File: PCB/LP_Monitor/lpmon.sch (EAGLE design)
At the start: 2 parts, among them U1 ATMEGA328P-PU

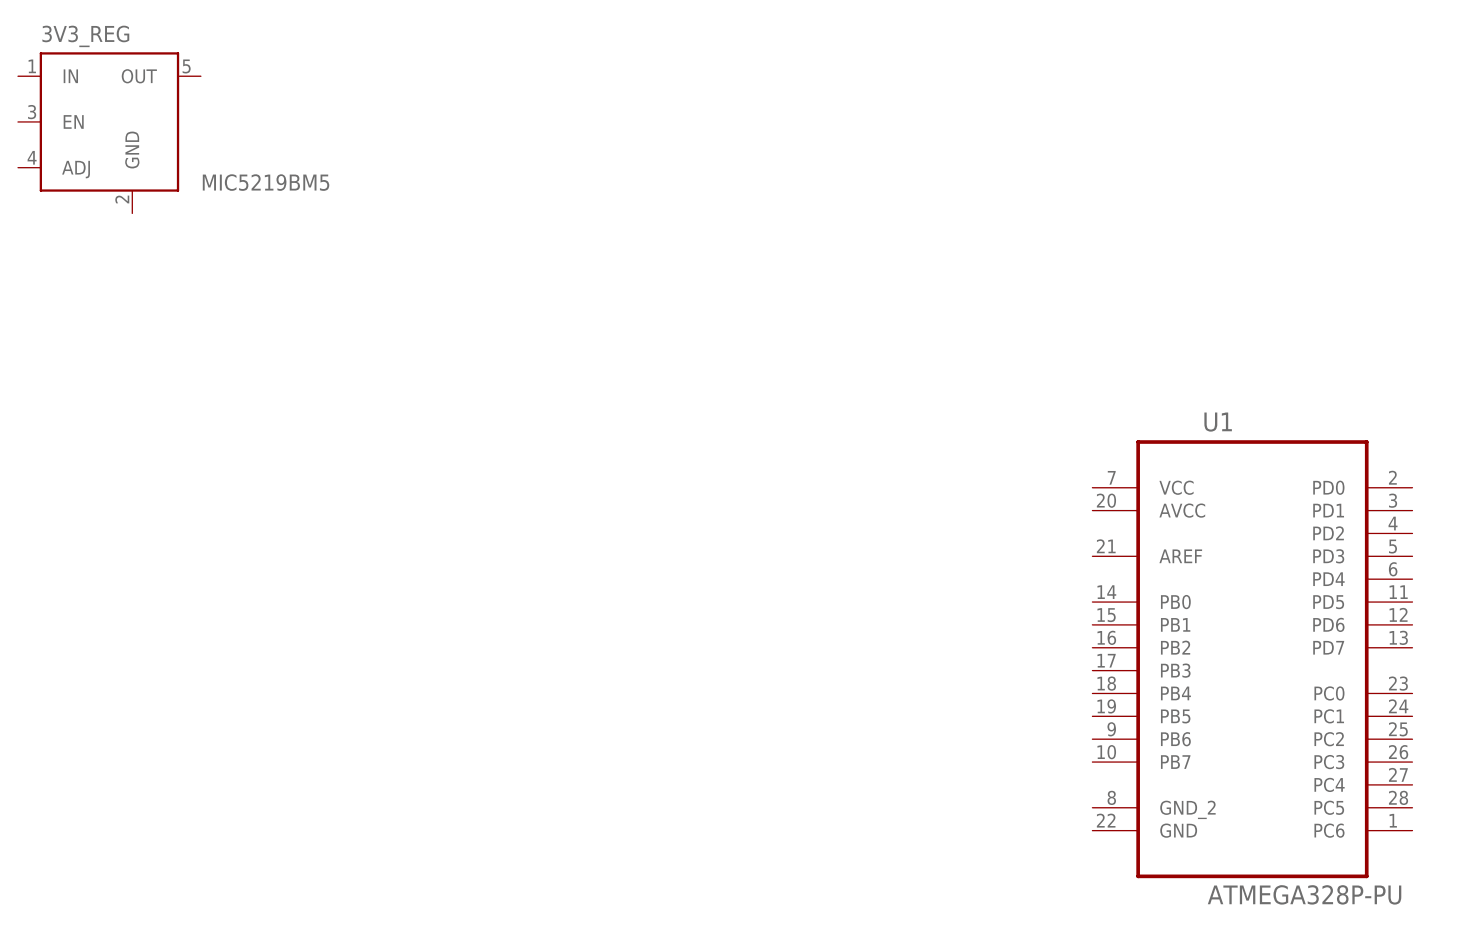
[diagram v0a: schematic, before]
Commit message: Arduino low power librarires
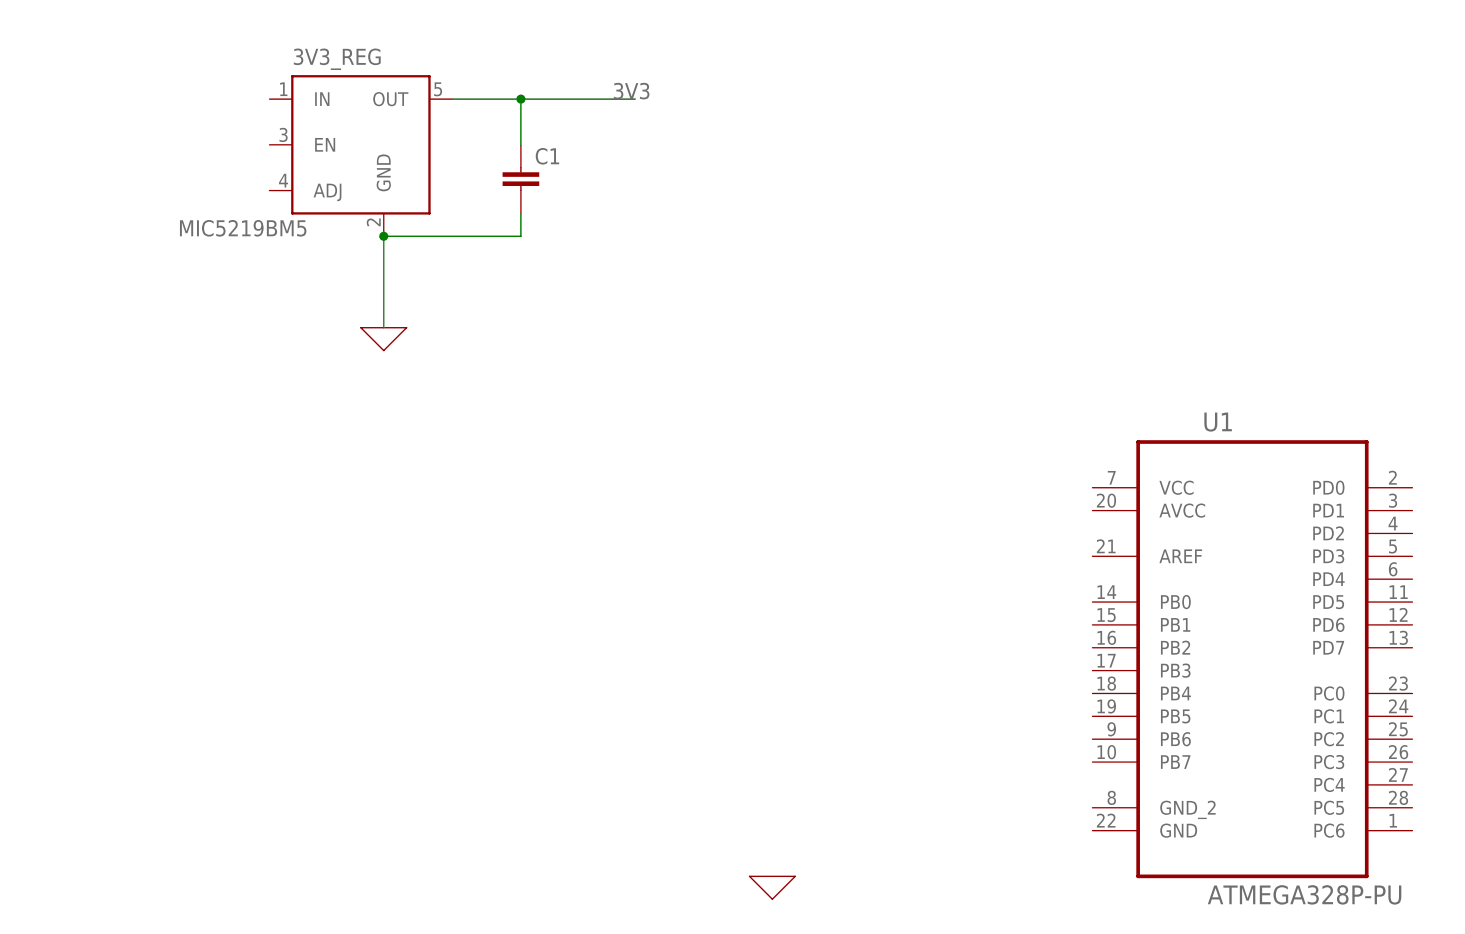
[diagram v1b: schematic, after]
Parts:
- added C1: (no value), capacitor-wima:C2.5/2
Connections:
- new net 0: 3V3_REG.GND, C1.2
- new net 3V3: 3V3_REG.OUT, C1.1
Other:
- moved on the sheet: 3V3_REG
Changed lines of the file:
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@@
 <layer number="97" name="Info" color="7" fill="1" visible="yes" active="yes"/>
 <layer number="98" name="Guide" color="6" fill="1" visible="yes" active="yes"/>
+<layer number="99" name="SpiceOrder" color="7" fill="1" visible="yes" active="yes"/>
 </layers>
 <schematic xreflabel="%F%N/%S.%C%R" xrefpart="/%S.%C%R">
@@
 <part name="U1" library="Atmel_By_element14_Batch_1-00" deviceset="ATMEGA328P-PU" device=""/>
 <part name="3V3_REG" library="v-reg-micrel" library_urn="urn:adsk.eagle:library:408" deviceset="MIC5219BM5" device="" package3d_urn="urn:adsk.eagle:package:30272/1"/>
+<part name="X_1" library="ngspice-simulation" library_urn="urn:adsk.eagle:library:527439" deviceset="GND" device=""/>
+<part name="X_2" library="ngspice-simulation" library_urn="urn:adsk.eagle:library:527439" deviceset="GND" device=""/>
+<part name="C1" library="capacitor-wima" library_urn="urn:adsk.eagle:library:116" deviceset="C" device="2.5/2" package3d_urn="urn:adsk.eagle:package:5415/1"/>
 </parts>
 <sheets>
@@
 <attribute name="VALUE" x="58.5216" y="32.4612" size="2.0828" layer="96" ratio="10" rot="SR0"/>
 </instance>
-<instance part="3V3_REG" gate="G1" x="-63.5" y="119.38" smashed="yes">
-<attribute name="NAME" x="-71.12" y="128.27" size="1.778" layer="95"/>
-<attribute name="VALUE" x="-53.34" y="111.76" size="1.778" layer="96"/>
+<instance part="3V3_REG" gate="G1" x="-35.56" y="116.84" smashed="yes">
+<attribute name="NAME" x="-43.18" y="125.73" size="1.778" layer="95"/>
+<attribute name="VALUE" x="-55.88" y="106.68" size="1.778" layer="96"/>
+</instance>
+<instance part="X_1" gate="G$1" x="-33.02" y="96.52" smashed="yes"/>
+<instance part="X_2" gate="G$1" x="10.16" y="35.56" smashed="yes"/>
+<instance part="C1" gate="G$1" x="-17.78" y="114.3" smashed="yes">
+<attribute name="NAME" x="-16.256" y="114.681" size="1.778" layer="95"/>
+<attribute name="VALUE" x="-16.256" y="109.601" size="1.778" layer="96"/>
 </instance>
 </instances>
@@
 </busses>
 <nets>
+<net name="0" class="0">
+<segment>
+<pinref part="X_1" gate="G$1" pin="0"/>
+<pinref part="3V3_REG" gate="G1" pin="GND"/>
+<wire x1="-33.02" y1="96.52" x2="-33.02" y2="106.68" width="0.1524" layer="91"/>
+<wire x1="-33.02" y1="106.68" x2="-17.78" y2="106.68" width="0.1524" layer="91"/>
+<junction x="-33.02" y="106.68"/>
+<wire x1="-17.78" y1="106.68" x2="-17.78" y2="109.22" width="0.1524" layer="91"/>
+<pinref part="C1" gate="G$1" pin="2"/>
+</segment>
+</net>
+<net name="3V3" class="0">
+<segment>
+<pinref part="3V3_REG" gate="G1" pin="OUT"/>
+<wire x1="-25.4" y1="121.92" x2="-17.78" y2="121.92" width="0.1524" layer="91"/>
+<label x="-7.62" y="121.92" size="1.778" layer="95"/>
+<wire x1="-17.78" y1="121.92" x2="-5.08" y2="121.92" width="0.1524" layer="91"/>
+<wire x1="-17.78" y1="116.84" x2="-17.78" y2="121.92" width="0.1524" layer="91"/>
+<junction x="-17.78" y="121.92"/>
+<pinref part="C1" gate="G$1" pin="1"/>
+</segment>
+</net>
 </nets>
 </sheet>
